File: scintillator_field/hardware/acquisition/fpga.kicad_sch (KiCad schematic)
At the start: 2 parts, among them U1 ICE40UP5K-SG48ITR, U12 W25Q16JVUXIQ

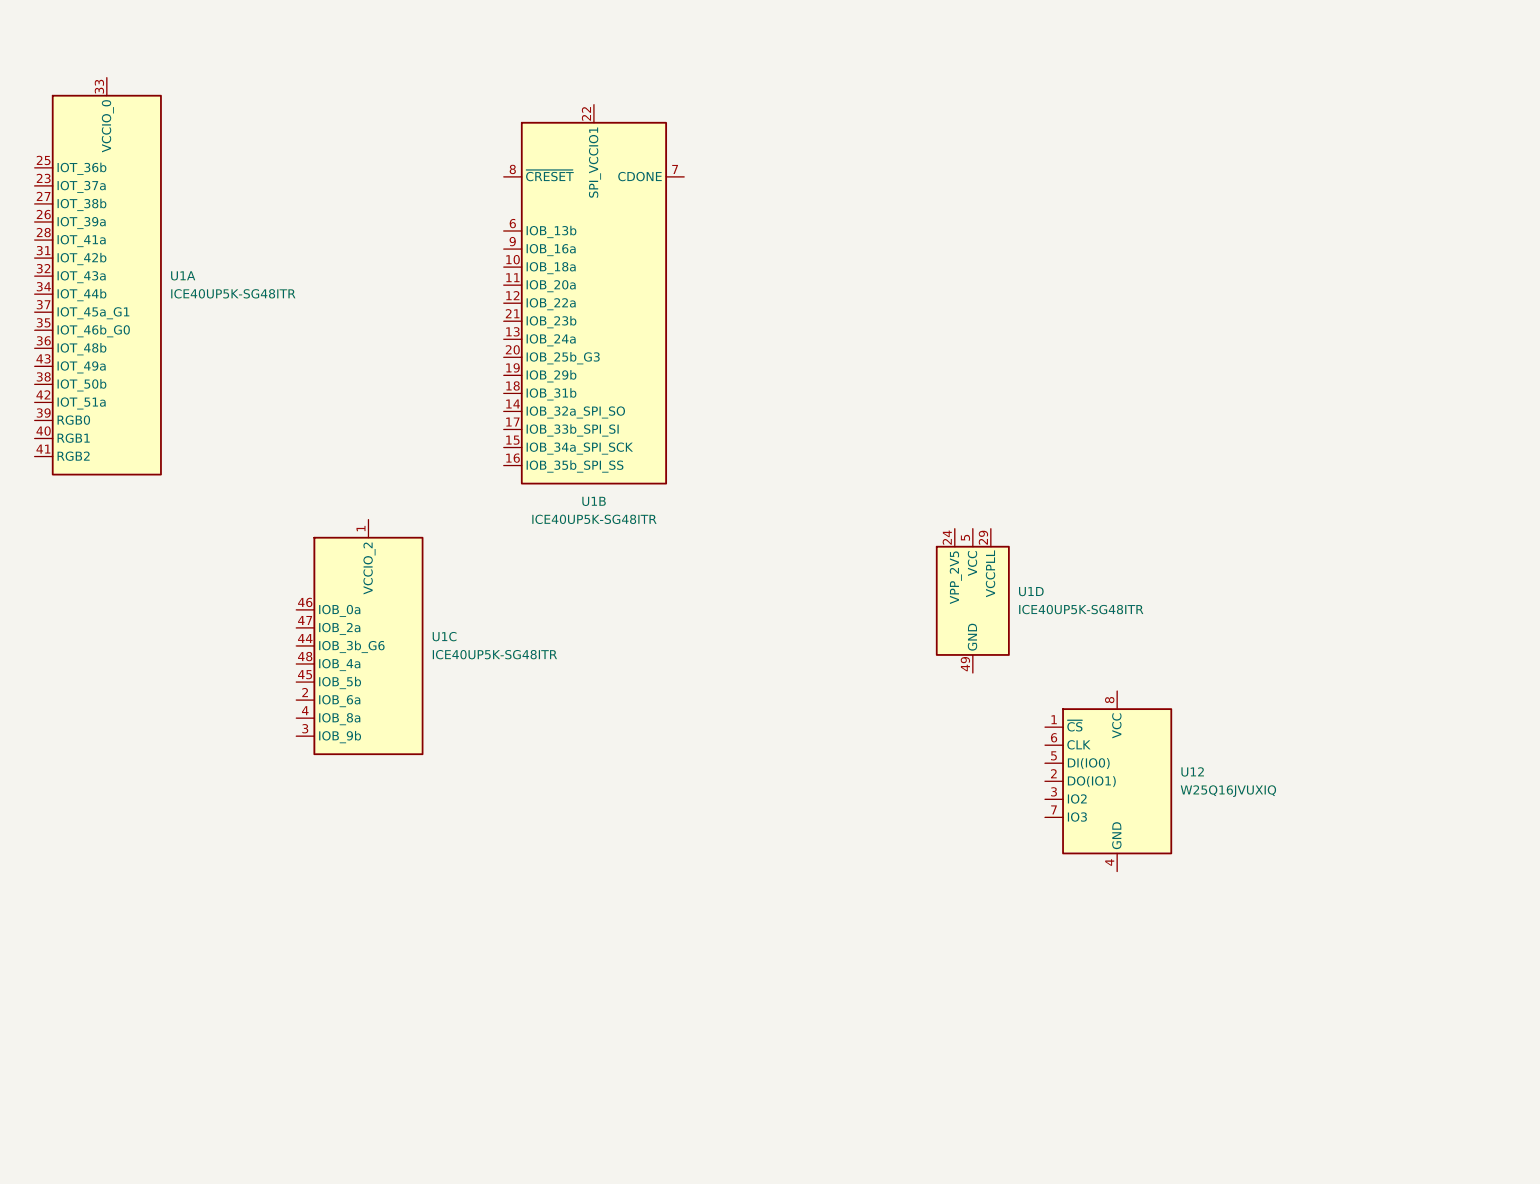
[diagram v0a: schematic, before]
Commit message: acquisition v2 basics
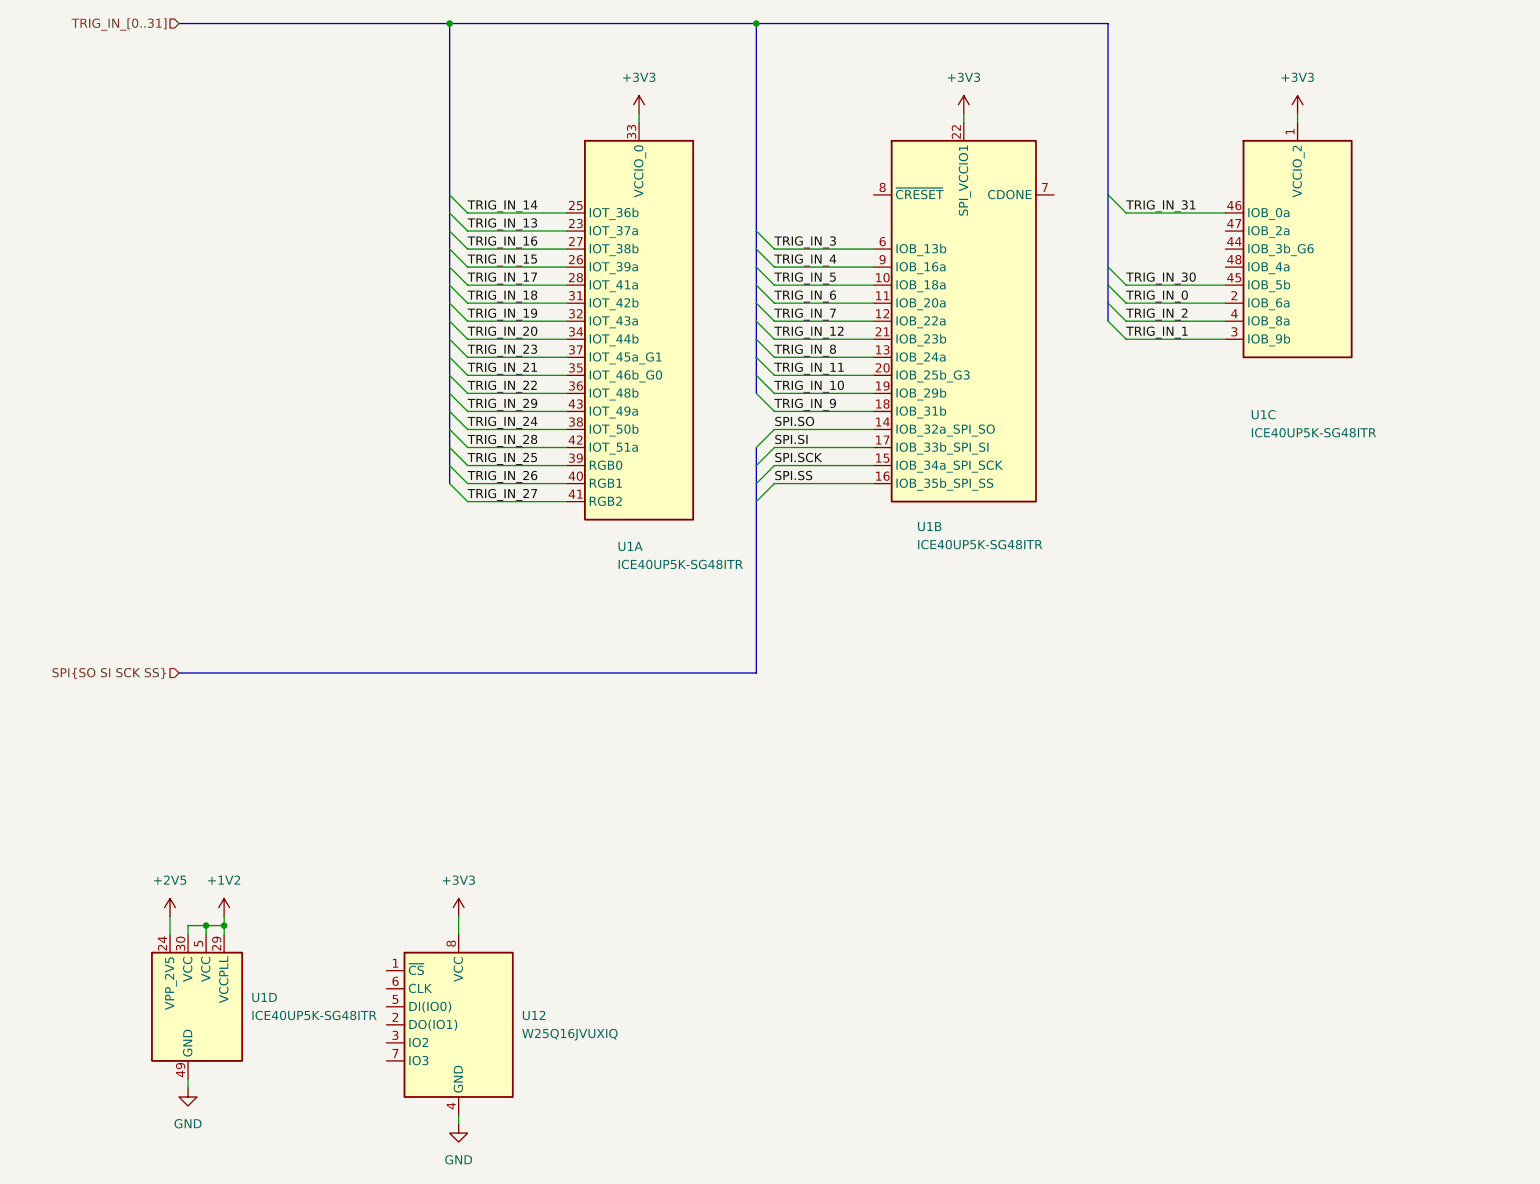
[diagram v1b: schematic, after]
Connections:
- net +2V5: now reaches U1.24 (VPP_2V5)
- net +1V2: now reaches U1.29 (VCCPLL)
- net +1V2: now also U1.30 (VCC), U1.5 (VCC)
- net GND: now reaches U1.49 (GND)
- net GND: now also U12.4 (GND)
- net TRIG_IN_13: now reaches U1.23 (IOT_37a)
- net TRIG_IN_14: now reaches U1.25 (IOT_36b)
- net TRIG_IN_15: now reaches U1.26 (IOT_39a)
- net TRIG_IN_16: now reaches U1.27 (IOT_38b)
- net TRIG_IN_17: now reaches U1.28 (IOT_41a)
- net TRIG_IN_18: now reaches U1.31 (IOT_42b)
- net TRIG_IN_19: now reaches U1.32 (IOT_43a)
- net +3V3: now reaches U1.33 (VCCIO_0)
- net +3V3: now also U1.1 (VCCIO_2), U1.22 (SPI_VCCIO1), U12.8 (VCC)
- net TRIG_IN_20: now reaches U1.34 (IOT_44b)
- net TRIG_IN_21: now reaches U1.35 (IOT_46b_G0)
- net TRIG_IN_22: now reaches U1.36 (IOT_48b)
- net TRIG_IN_23: now reaches U1.37 (IOT_45a_G1)
- net TRIG_IN_24: now reaches U1.38 (IOT_50b)
- net TRIG_IN_25: now reaches U1.39 (RGB0)
- net TRIG_IN_26: now reaches U1.40 (RGB1)
- net TRIG_IN_27: now reaches U1.41 (RGB2)
- net TRIG_IN_28: now reaches U1.42 (IOT_51a)
- net TRIG_IN_29: now reaches U1.43 (IOT_49a)
- net TRIG_IN_0: now reaches U1.2 (IOB_6a)
- net TRIG_IN_1: now reaches U1.3 (IOB_9b)
- net TRIG_IN_2: now reaches U1.4 (IOB_8a)
- net TRIG_IN_30: now reaches U1.45 (IOB_5b)
- net TRIG_IN_31: now reaches U1.46 (IOB_0a)
- net TRIG_IN_5: now reaches U1.10 (IOB_18a)
- net TRIG_IN_6: now reaches U1.11 (IOB_20a)
- net TRIG_IN_7: now reaches U1.12 (IOB_22a)
- net TRIG_IN_8: now reaches U1.13 (IOB_24a)
- net SPI.SO: now reaches U1.14 (IOB_32a_SPI_SO)
- net SPI.SCK: now reaches U1.15 (IOB_34a_SPI_SCK)
- net SPI.SS: now reaches U1.16 (IOB_35b_SPI_SS)
- net SPI.SI: now reaches U1.17 (IOB_33b_SPI_SI)
- net TRIG_IN_9: now reaches U1.18 (IOB_31b)
- net TRIG_IN_10: now reaches U1.19 (IOB_29b)
- net TRIG_IN_11: now reaches U1.20 (IOB_25b_G3)
- net TRIG_IN_12: now reaches U1.21 (IOB_23b)
- net TRIG_IN_3: now reaches U1.6 (IOB_13b)
- net TRIG_IN_4: now reaches U1.9 (IOB_16a)
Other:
- moved on the sheet: U12, U1A, U1B, U1C

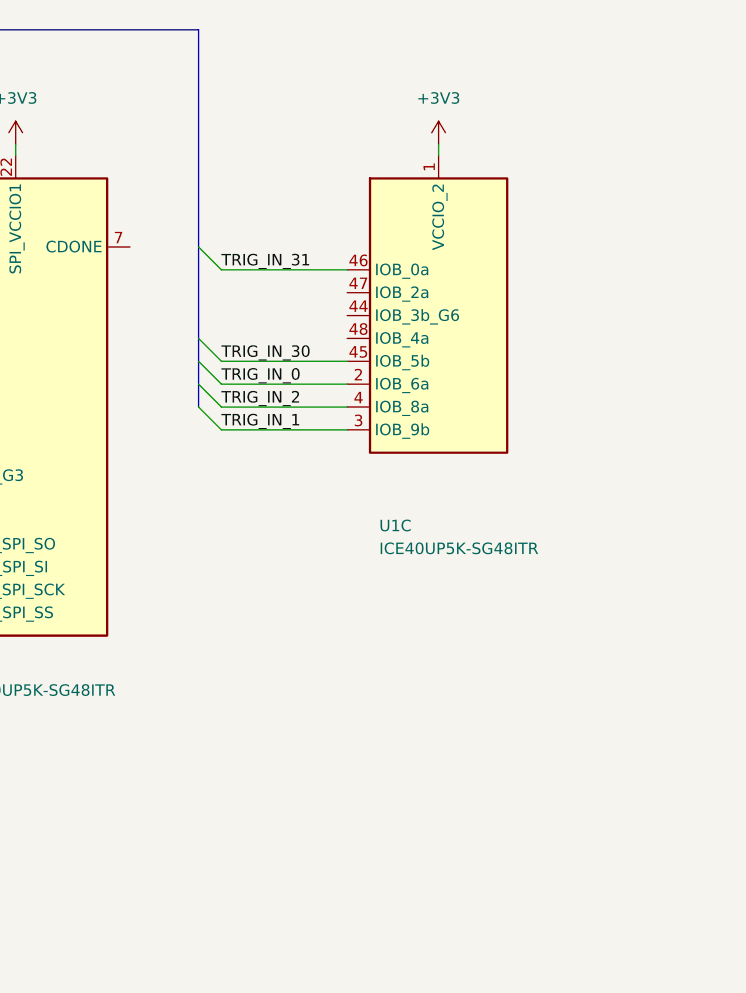
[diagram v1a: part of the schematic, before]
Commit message: 24 mhz oscillator
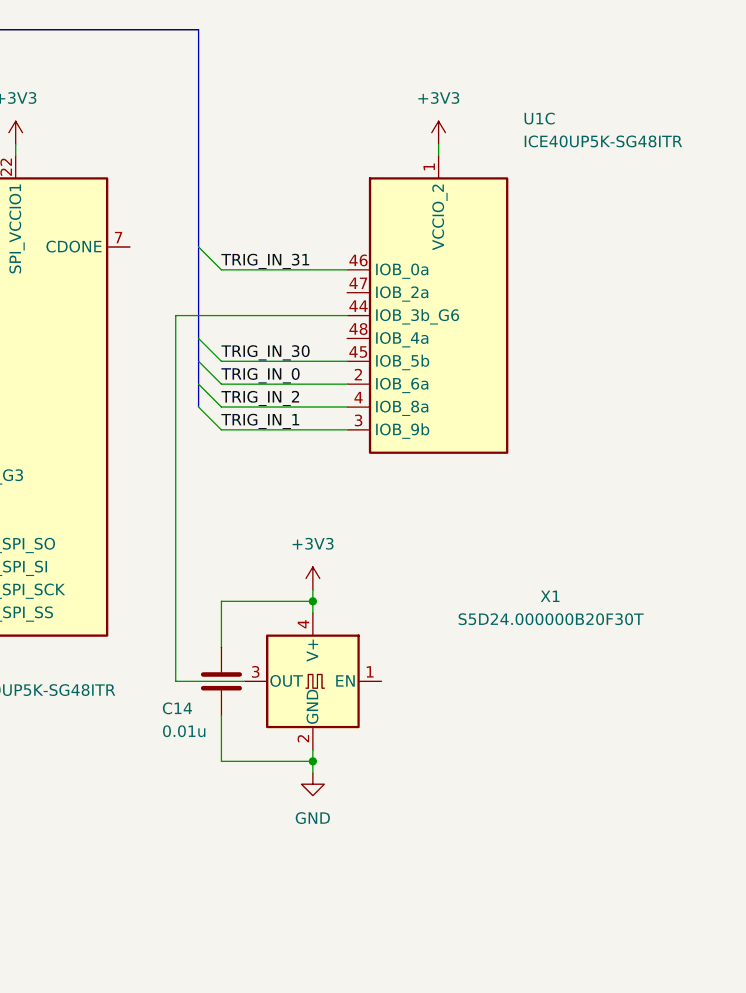
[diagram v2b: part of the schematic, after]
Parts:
- added C14: 0.01u, symbol Device:C
- added X1: S5D24.000000B20F30T, Oscillator:Oscillator_SMD_EuroQuartz_XO32-4Pin_3.2x2.5mm, symbol s5d24:S5D24.000000B20F30T
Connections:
- net +3V3: now also C14.1, X1.4 (V+)
- net GND: now also C14.2, X1.2 (GND)
- net at U1.44 (IOB_3b_G6): now also X1.3 (OUT)
